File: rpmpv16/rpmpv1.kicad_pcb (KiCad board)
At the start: 2 copper layers, 99.4 x 64.4 mm, 19 parts, among them J1 RPi_GPIO, J2 Conn_01x04, P1 CONN_02X25, U1 74HC244, U2 74HC244, U3 74LS07, U4 74HC244, U5 LVC4245

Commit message: update for new kicad but not perfect
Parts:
- added U6: 74HC00, Package_SO:SOIC-14_3.9x8.7mm_P1.27mm, B.Cu at (129.5, 67.3)
- J2: footprint Pin_Headers:Pin_Header_Straight_1x04_Pitch2.54mm -> Connector_PinHeader_2.54mm:PinHeader_1x04_P2.54mm_Horizontal
- U3: footprint Housings_SOIC:SOIC-14_3.9x8.7mm_Pitch1.27mm -> Package_SO:SOIC-14_3.9x8.7mm_P1.27mm
- moved U3 5.94 mm to (118.1, 67.3)
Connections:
- U3 pad 1: /RC23 -> /CWAIT
- U3 pad 2: /INT -> /WAIT
- U3 pad 3: /DAT_DIR -> /RC23
- U3 pad 4: /BUSDIR -> /INT
- U3 pad 5: (no net) -> /DAT_DIR
- U3 pad 6: (no net) -> /BUSDIR
- U3 pad 8: /WAIT -> (no net)
- U3 pad 9: /RC24 -> (no net)
- U4 pad 11: /RESET -> Net-(U4-Pad11)
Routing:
- net /A13: track 62.1 -> 129.3 mm
- net /RESET: track 66.0 -> 0.00 mm, vias 2 -> 0
- net /MREQ: track 66.4 -> 120.0 mm
- net /RD7: track 68.4 -> 114.7 mm
- net /WAIT: track 135.7 -> 90.6 mm, vias 0 -> 2
- net /CLK: track 61.1 -> 95.0 mm, vias 3 -> 1
- net /BUSDIR: track 114.1 -> 83.5 mm, vias 1 -> 3
- net /INT: track 114.0 -> 88.4 mm, vias 1 -> 3
- net /DAT_EN: track 67.1 -> 90.9 mm, vias 2 -> 1
- net /RC23: track 64.6 -> 80.5 mm, vias 0 -> 1
- net /A0: track 60.2 -> 75.7 mm
- net /CWAIT: track 0.00 -> 14.1 mm
- net /A14: track 53.4 -> 66.4 mm
- net /IORQ: track 62.8 -> 75.1 mm, vias 2 -> 0
- net /A11: track 58.3 -> 46.2 mm
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
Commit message: new board with lichee pi nano
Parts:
- removed G3: LOGO, MSX:raspberry_pi_logo
- removed J1: RPi_GPIO, Socket_Strips:Socket_Strip_Angled_2x20_Pitch2.54mm
- added R6: R, Resistor_SMD:R_0805_2012Metric_Pad1.15x1.40mm_HandSolder, B.Cu at (111.9, 52.7)
- added R7: R, Resistor_SMD:R_0805_2012Metric_Pad1.15x1.40mm_HandSolder, B.Cu at (111.9, 55.2)
- C1: footprint Capacitors_SMD:CP_Elec_4x4.5 -> Capacitor_THT:CP_Radial_Tantal_D5.0mm_P5.00mm
- C2: footprint Capacitors_SMD:C_0603_HandSoldering -> Capacitor_SMD:C_0805_2012Metric_Pad1.15x1.40mm_HandSolder
- R1, R2, R3, R4, R5: footprint Resistors_SMD:R_0603_HandSoldering -> Resistor_SMD:R_0805_2012Metric_Pad1.15x1.40mm_HandSolder
- U6: value 74HC00 -> licheepi_nano; footprint Package_SO:SOIC-14_3.9x8.7mm_P1.27mm -> MSX:licheepi_nano; moved to F.Cu
- moved U6 57.0 mm to (186.6, 66.5)
- moved U3 47.5 mm to (159.8, 90.2), turned to 90 degrees
- moved U1 45.9 mm to (175.3, 90.2)
- moved U4 43.9 mm to (175.3, 90.2)
- moved G1 33.0 mm to (114.6, 78.8)
- moved G2 29.9 mm to (144.9, 56.4)
- moved U2 29.9 mm to (142.2, 90.2)
- moved U5 28.6 mm to (142.2, 90.2)
- moved R5 2.54 mm to (119.2, 94.7)
- moved C1 2.45 mm to (116.8, 98.2)
- moved R3 0.51 mm to (121.6, 56.3)
- moved R1 0.51 mm to (121.6, 51.8)
- moved J2 0.06 mm to (108.3, 52.7)
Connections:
- C2 pad 1: GND -> Net-(C2-Pad1)
- J2 pad 1: /RD2 -> /SDA
- J2 pad 2: /RD3 -> /SCK
- J2 pad 3: +3V3 -> /VCC
- J2 pad 4: GND -> /GND
- P1 pad 41: GND -> /GND
- P1 pad 43: GND -> /GND
- P1 pad 45: +5V -> /5V0
- P1 pad 47: +5V -> /5V0
- R1 pad 2: +3V3 -> /VCC
- R2 pad 2: +3V3 -> /VCC
- R3 pad 2: +3V3 -> /VCC
- R5 pad 1: GND -> Net-(C2-Pad1)
- U1 pad 10: GND -> /GND
- U1 pad 20: +3V3 -> /VCC
- U2 pad 10: GND -> /GND
- U2 pad 20: +3V3 -> /VCC
- U3 pad 1: /CWAIT -> /RWAIT
- U3 pad 14: +3V3 -> (no net)
- U3 pad 3: /RC23 -> /RINT
- U3 pad 7: GND -> (no net)
- U4 pad 1: GND -> /GND
- U4 pad 10: GND -> /GND
- U4 pad 11: Net-(U4-Pad11) -> /M1
- U4 pad 12: /RC20 -> /RMREQ
- U4 pad 14: /RC27 -> /RIORQ
- U4 pad 15: /MREQ -> /WR
- U4 pad 16: /RC21 -> /RCLK
- U4 pad 17: /IORQ -> /RD
- U4 pad 18: Net-(U4-Pad18) -> /RRST
- U4 pad 19: GND -> /DAT_EN
- U4 pad 2: /CLK -> /RESET
- U4 pad 20: +3V3 -> /VCC
- U4 pad 3: /RC19 -> /RA8
- U4 pad 4: /M1 -> /CLK
- U4 pad 5: /RC26 -> /RA9
- U4 pad 6: /WR -> /IORQ
- U4 pad 7: /RC17 -> /RA11
- U4 pad 8: /RD -> /MREQ
- U4 pad 9: Net-(U4-Pad9) -> /RA10
- U5 pad 1: +5V -> /5V0
- U5 pad 11: GND -> /GND
- U5 pad 12: GND -> /GND
- U5 pad 13: GND -> /GND
- U5 pad 23: +3V3 -> /VCC
- U5 pad 24: +3V3 -> /VCC
- U6 pad 1: /IORQ -> Net-(U6-Pad1)
- U6 pad 10: (no net) -> /GND
- U6 pad 11: (no net) -> /VCC
- U6 pad 12: (no net) -> Net-(U6-Pad12)
- U6 pad 13: (no net) -> Net-(U6-Pad13)
- U6 pad 14: +3V3 -> Net-(U6-Pad14)
- U6 pad 2: /MREQ -> /RRST
- U6 pad 4: Net-(U6-Pad3) -> Net-(U6-Pad4)
- U6 pad 5: /RC24 -> /TVOUT
- U6 pad 6: /CWAIT -> Net-(U6-Pad6)
- U6 pad 7: GND -> Net-(U6-Pad7)
- U6 pad 8: (no net) -> /5V0
- U6 pad 9: (no net) -> Net-(U6-Pad9)
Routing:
- net GND: track 218.7 -> 0.00 mm, vias 5 -> 0
- net /GND: track 0.00 -> 215.5 mm, vias 0 -> 3
- net +3V3: track 205.0 -> 0.00 mm, vias 3 -> 0
- net /VCC: track 0.00 -> 167.7 mm, vias 0 -> 3
- net /5V0: track 0.00 -> 127.1 mm, vias 0 -> 2
- net +5V: track 109.5 -> 0.00 mm, vias 3 -> 0
- net /MREQ: track 120.0 -> 17.2 mm
- net /SCK: track 0.00 -> 89.8 mm, vias 0 -> 1
- net /A13: track 129.3 -> 40.3 mm
- net /SDA: track 0.00 -> 85.1 mm, vias 0 -> 1
- net /RD2: track 127.9 -> 44.9 mm, vias 1 -> 2
- net /RC23: track 80.5 -> 0.00 mm, vias 1 -> 0
- net /RC18: track 160.7 -> 84.1 mm, vias 0 -> 1
- net /RD3: track 113.5 -> 42.6 mm, vias 1 -> 2
- net /RC24: track 70.1 -> 0.00 mm, vias 1 -> 0
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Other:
- outline, holes or cut-outs redrawn
- board text added: "2020.3.16"
- board text added: "RPMP-LICHEE"
- board text removed: "2020.1.14"
- board text removed: "RPMP"

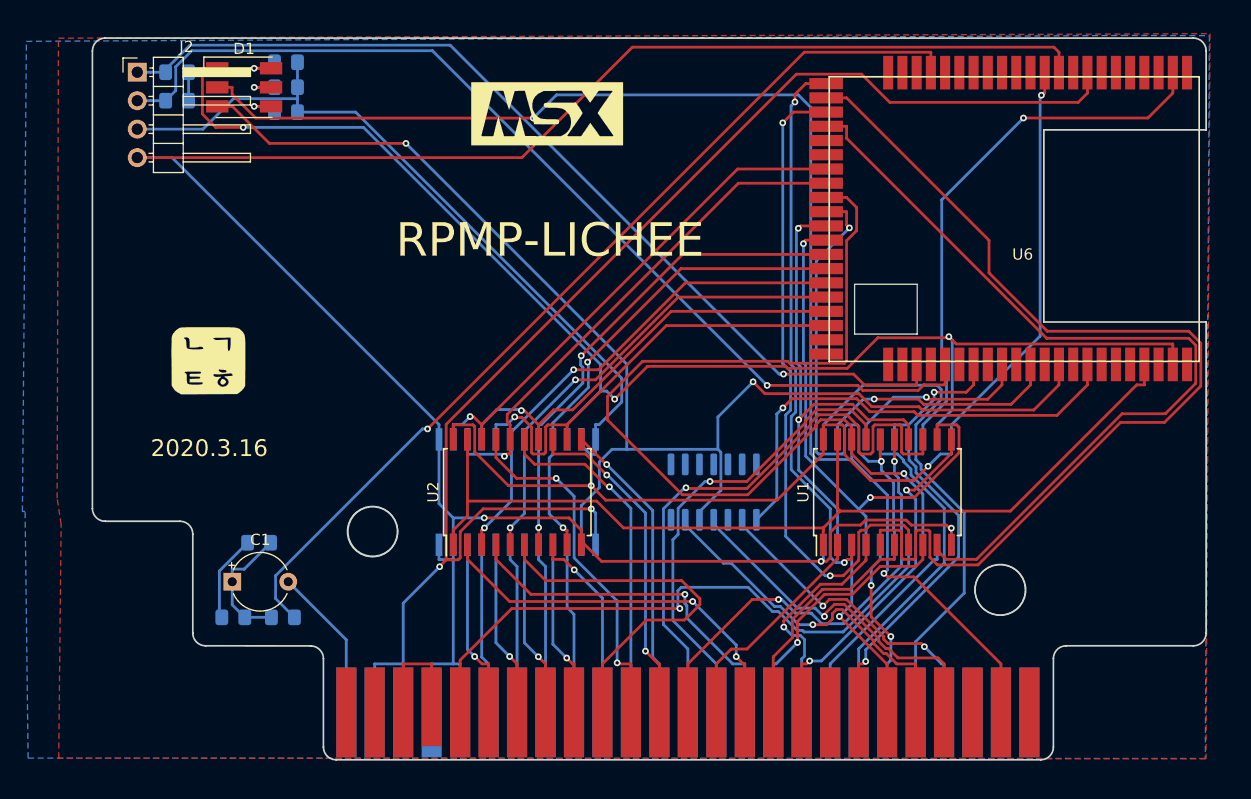
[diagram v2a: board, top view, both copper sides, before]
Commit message: updated for new PCB order
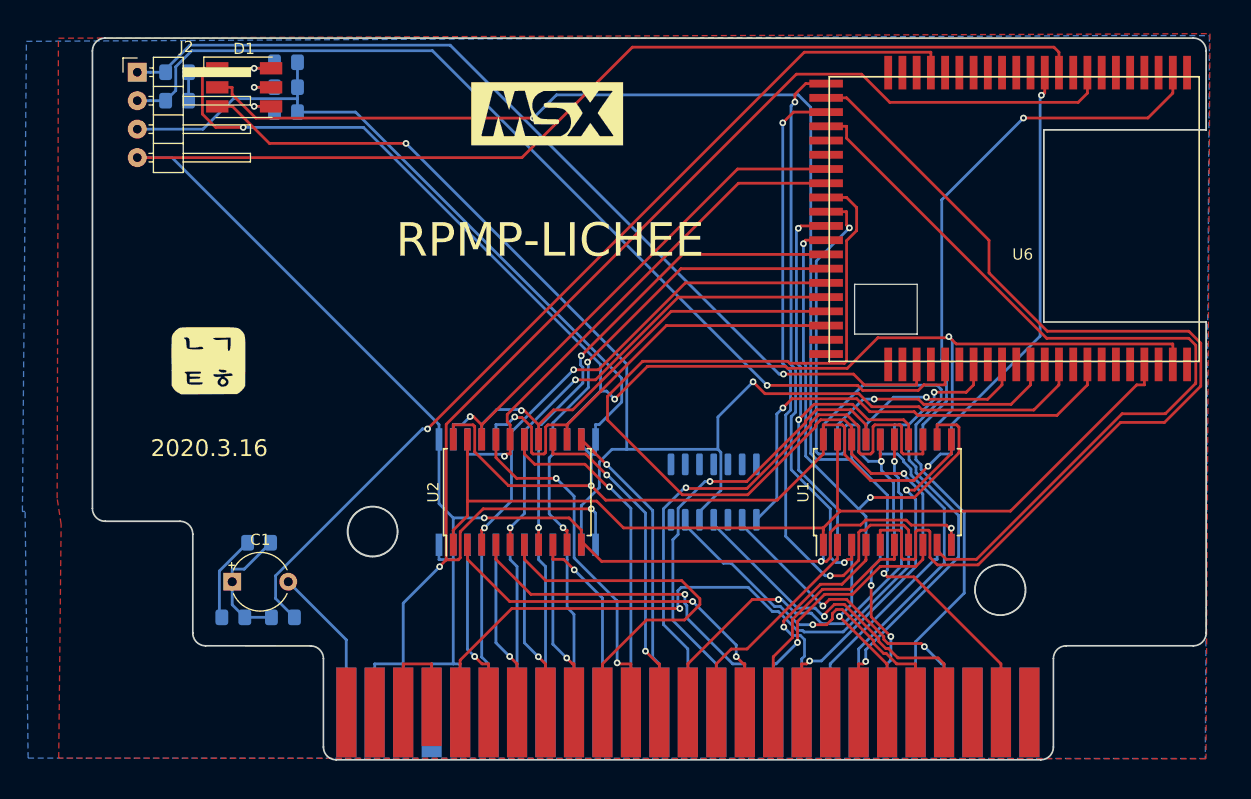
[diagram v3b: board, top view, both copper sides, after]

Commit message: more test pcb
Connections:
- C2 pad 1: Net-(C2-Pad1) -> /GND
- R5 pad 1: Net-(C2-Pad1) -> /GND
- R6 pad 1: /3V3 -> /VCC
- R7 pad 1: /3V3 -> /VCC
- U6 pad 12: Net-(U6-Pad12) -> /VCC
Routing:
- net /GND: track 215.5 -> 223.2 mm
- net Net-(C2-Pad1): track 7.79 -> 0.00 mm
- net /3V3: track 2.54 -> 0.00 mm
- net /VCC: track 167.7 -> 170.2 mm
- added copper zone on B.Cu, net /GND
- added copper zone on F.Cu, net /GND
- removed copper zone on B.Cu, net GND
- removed copper zone on F.Cu, net GND
